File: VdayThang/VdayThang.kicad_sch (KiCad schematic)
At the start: 35 parts, among them SW1 SW_DIP_x01, U1 ATtiny85-20S

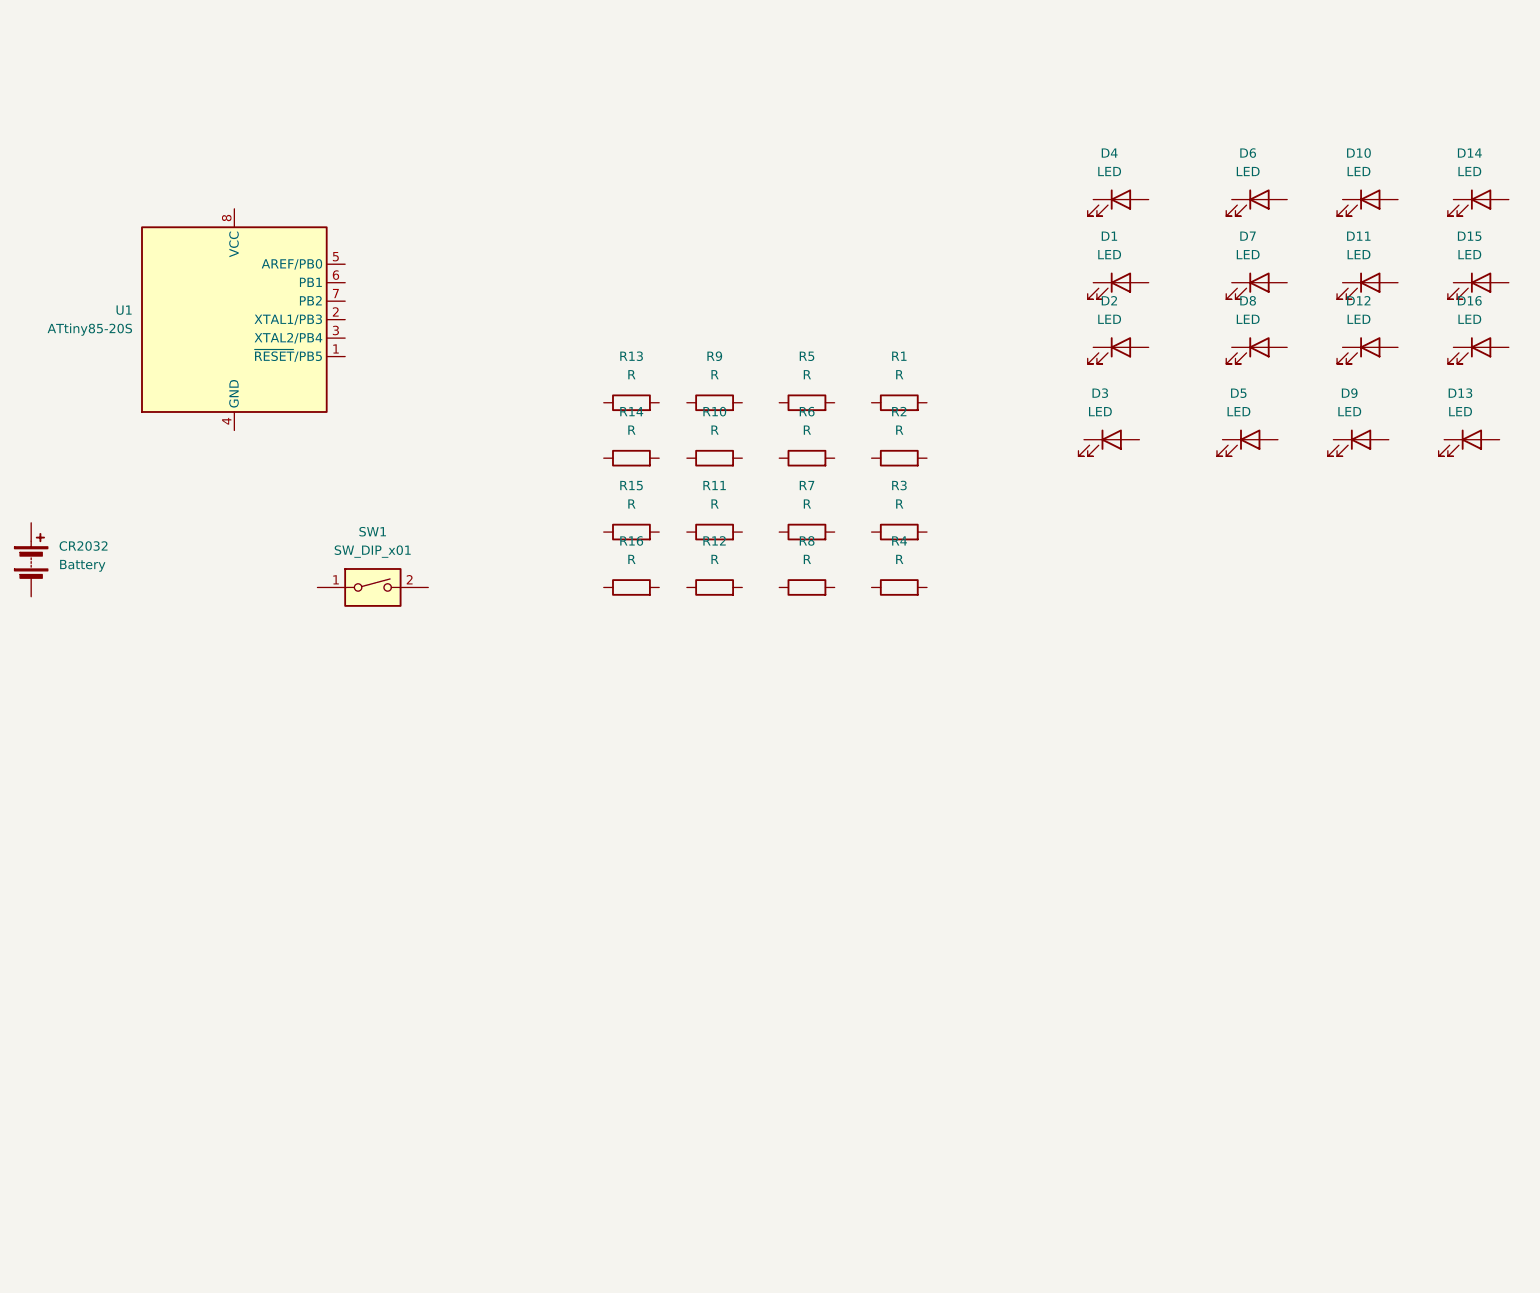
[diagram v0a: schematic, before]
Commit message: Schematic Mostly Done
Still need to assign footprints
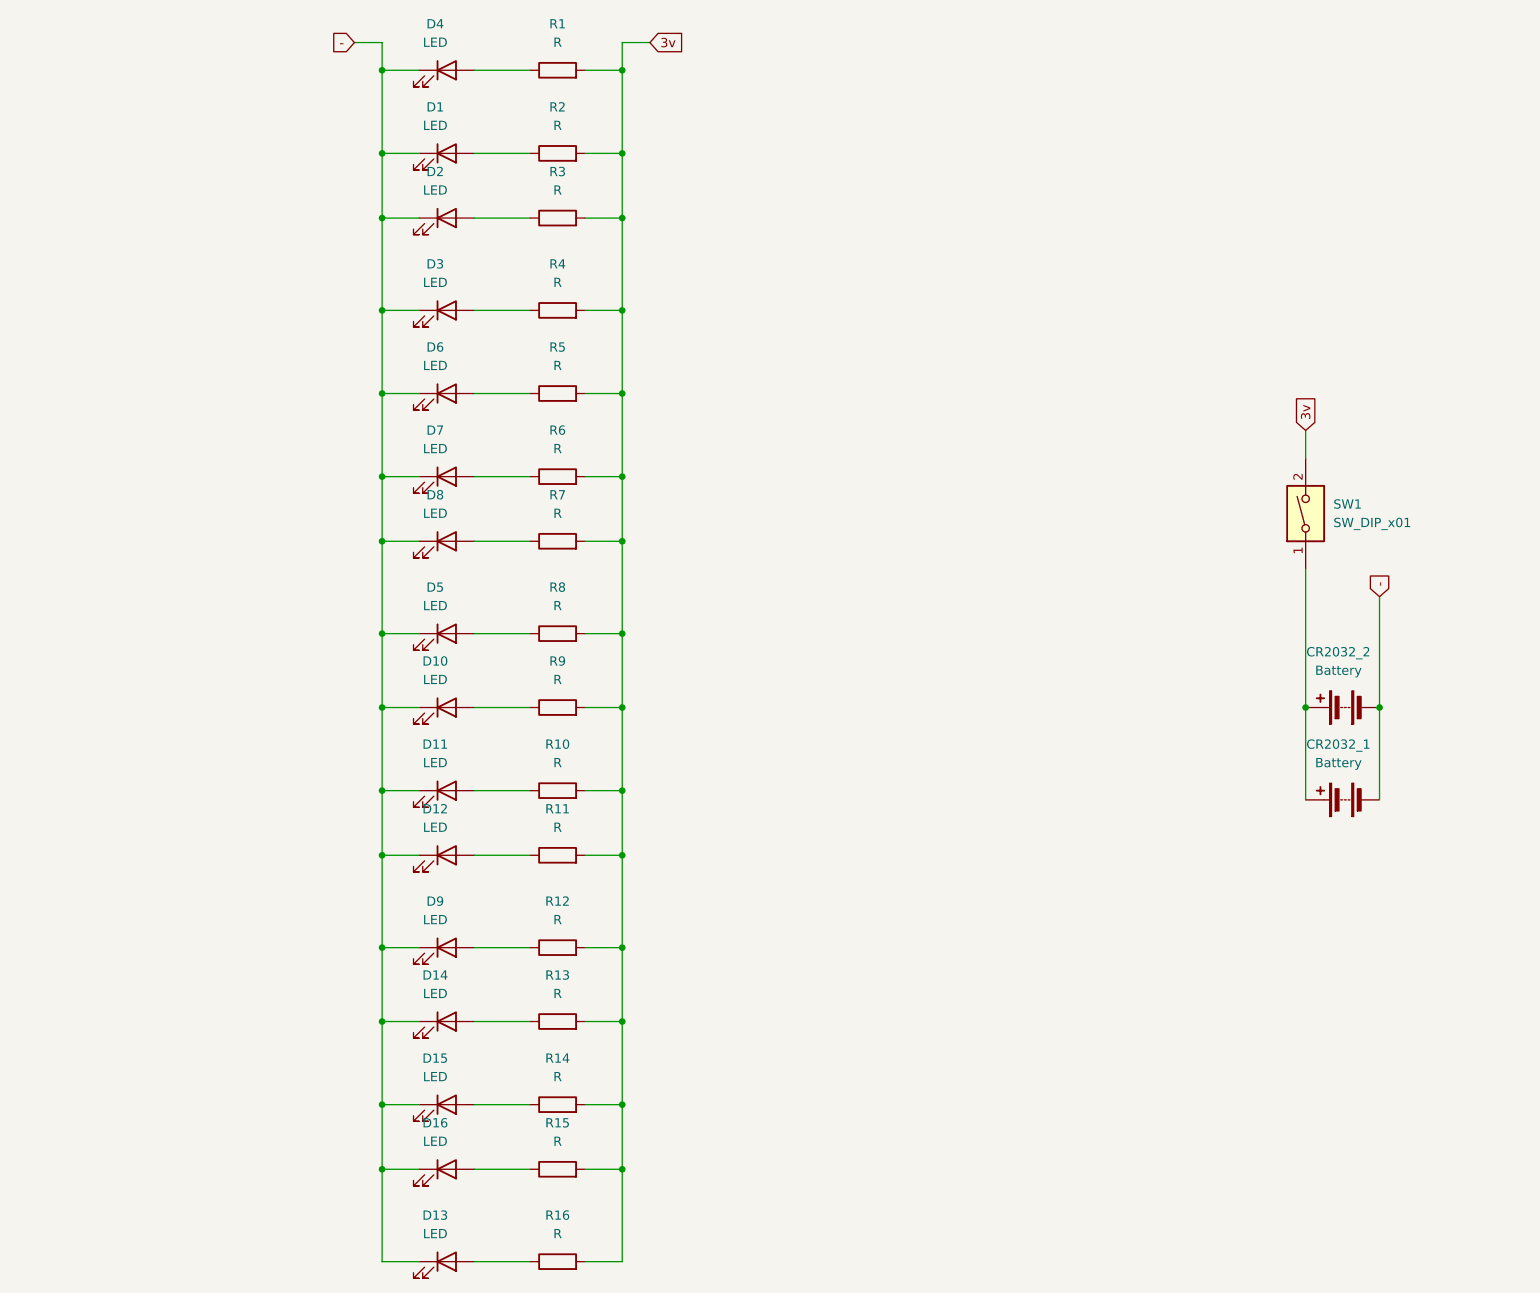
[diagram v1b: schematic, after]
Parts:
- removed U1: ATtiny85-20S, Package_SO:SOIC-8W_5.3x5.3mm_P1.27mm, symbol MCU_Microchip_ATtiny:ATtiny85-20S
- added CR2032_2: Battery, symbol Device:Battery
- renumbered CR2032 to CR2032_1
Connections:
- net -: now reaches D4.1 (K)
- net -: now also CR2032_1.2 (-), D1.1 (K), D10.1 (K), D11.1 (K), D12.1 (K), D13.1 (K), D14.1 (K), D15.1 (K), D16.1 (K), D2.1 (K), D3.1 (K), D5.1 (K), D6.1 (K), D7.1 (K), D8.1 (K), D9.1 (K), CR2032_2.2 (-)
- net at D4.2 (A): now also R1.1
- net at D1.2 (A): now also R2.1
- net at R12.1: now also D9.2 (A)
- net 3v: now reaches R12.2
- net 3v: now also R1.2, R10.2, R11.2, R13.2, R14.2, R15.2, R16.2, R2.2, R3.2, R4.2, R5.2, R6.2, R7.2, R8.2, R9.2, SW1.2
- net at D2.2 (A): now also R3.1
- net at CR2032_1.1 (+): now also SW1.1, CR2032_2.1 (+)
- net at R15.1: now also D16.2 (A)
- net at D7.2 (A): now also R6.1
- net at R5.1: now also D6.2 (A)
- net at D8.2 (A): now also R7.1
- net at D12.2 (A): now also R11.1
- net at R9.1: now also D10.2 (A)
- net at R13.1: now also D14.2 (A)
- net at R14.1: now also D15.2 (A)
- net at D11.2 (A): now also R10.1
- net at R8.1: now also D5.2 (A)
- net at R4.1: now also D3.2 (A)
- net at R16.1: now also D13.2 (A)
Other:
- title: (none) -> LED Heart
- moved on the sheet: CR2032_1, D1, D10, D11, D12, D13, D14, D15, D16, D2, D3, D4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

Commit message: assigned footprints
assigned footprints
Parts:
- removed SW1: SW_DIP_x01, symbol Switch:SW_DIP_x01
- added S1: SLW-66527511-SMT-TR, LogansCustom:SW_SLW-66527511-SMT-TR, symbol logancustom:SLW-66527511-SMT-TR
- CR2032_1, CR2032_2: footprint (none) -> LogansCustom:BAT_CR2032
- D1, D10, D11, D12, D13, D14, D15, D16, D2, D3, D4, D5, D6, D7, D8, D9: footprint (none) -> LED_SMD:LED_0805_2012Metric
- R1, R10, R11, R12, R13, R14, R15, R16, R2, R3, R4, R5, R6, R7, R8, R9: footprint (none) -> Resistor_SMD:R_0805_2012Metric
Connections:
- net 3v: now also S1.3
- net at CR2032_1.1 (+), CR2032_2.1 (+): now also S1.2

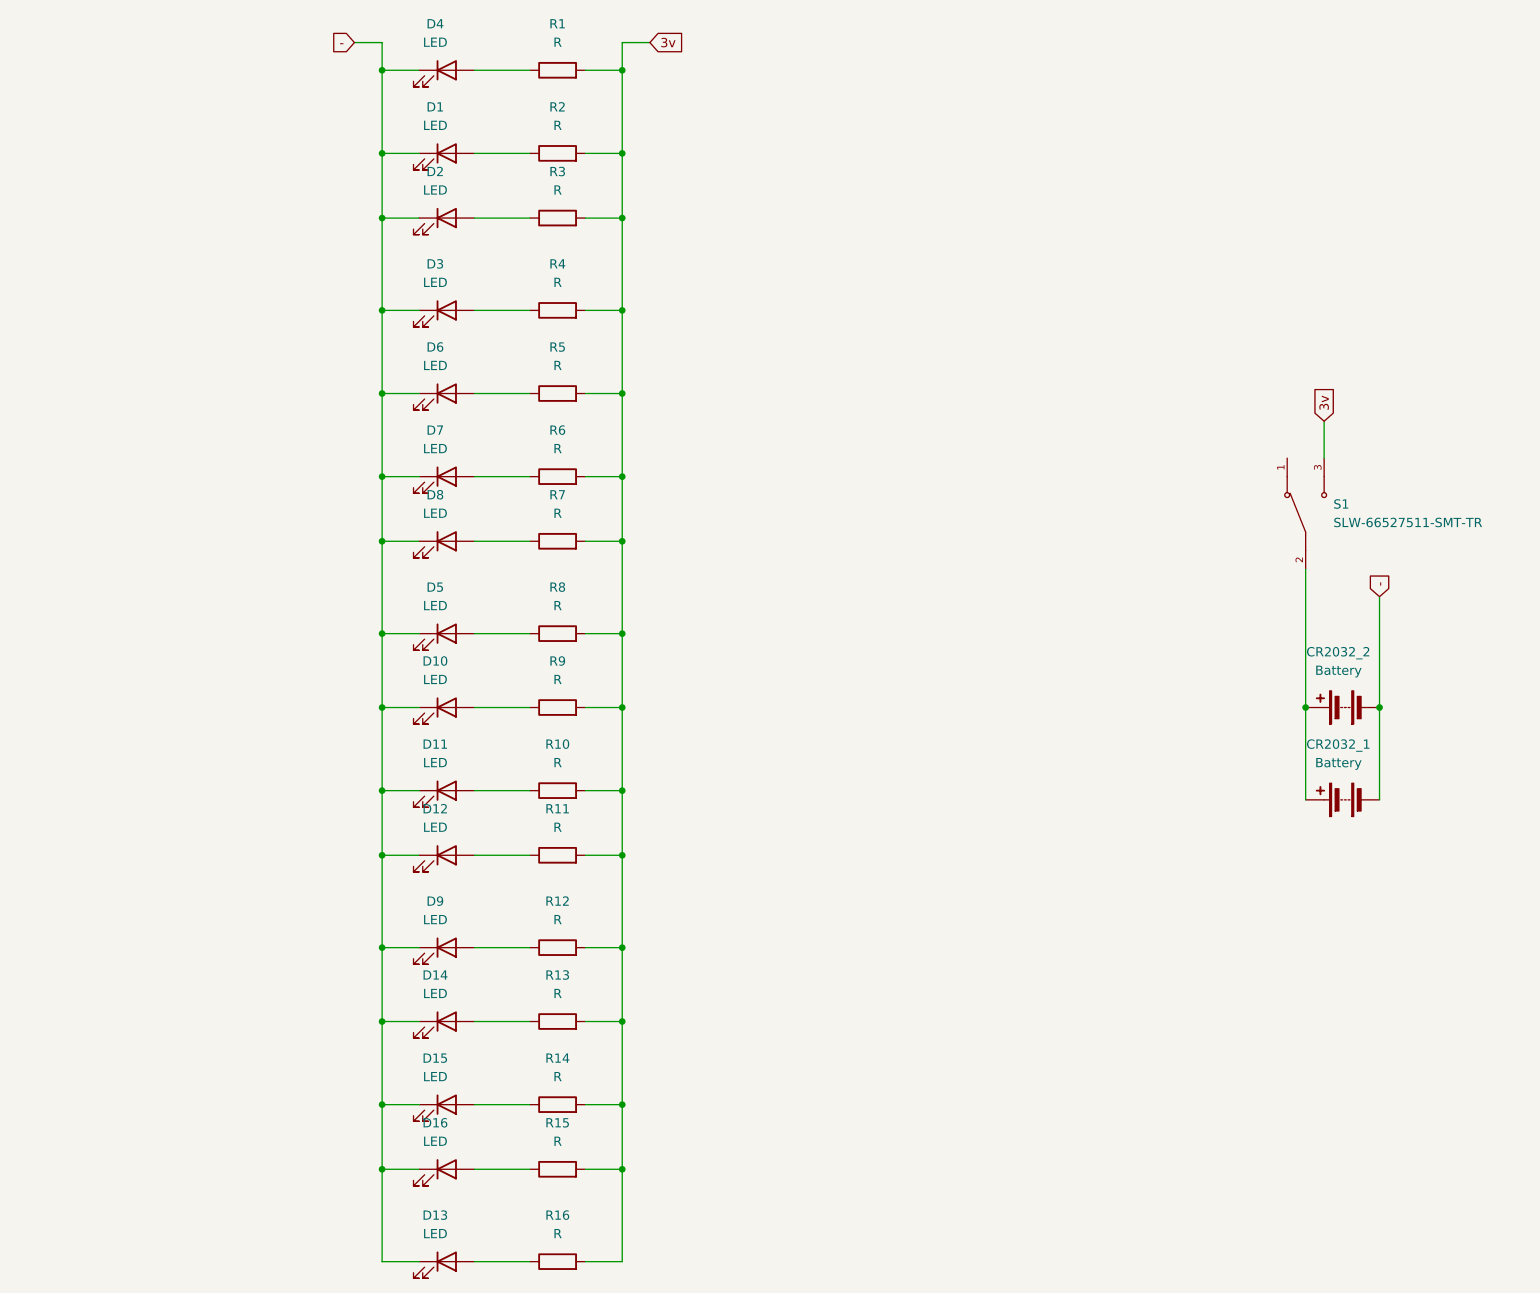
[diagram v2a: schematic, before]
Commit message: Routing and Footprints done
Finished routing board, made cr2032 holder footprint. Still need to add edge cuts.
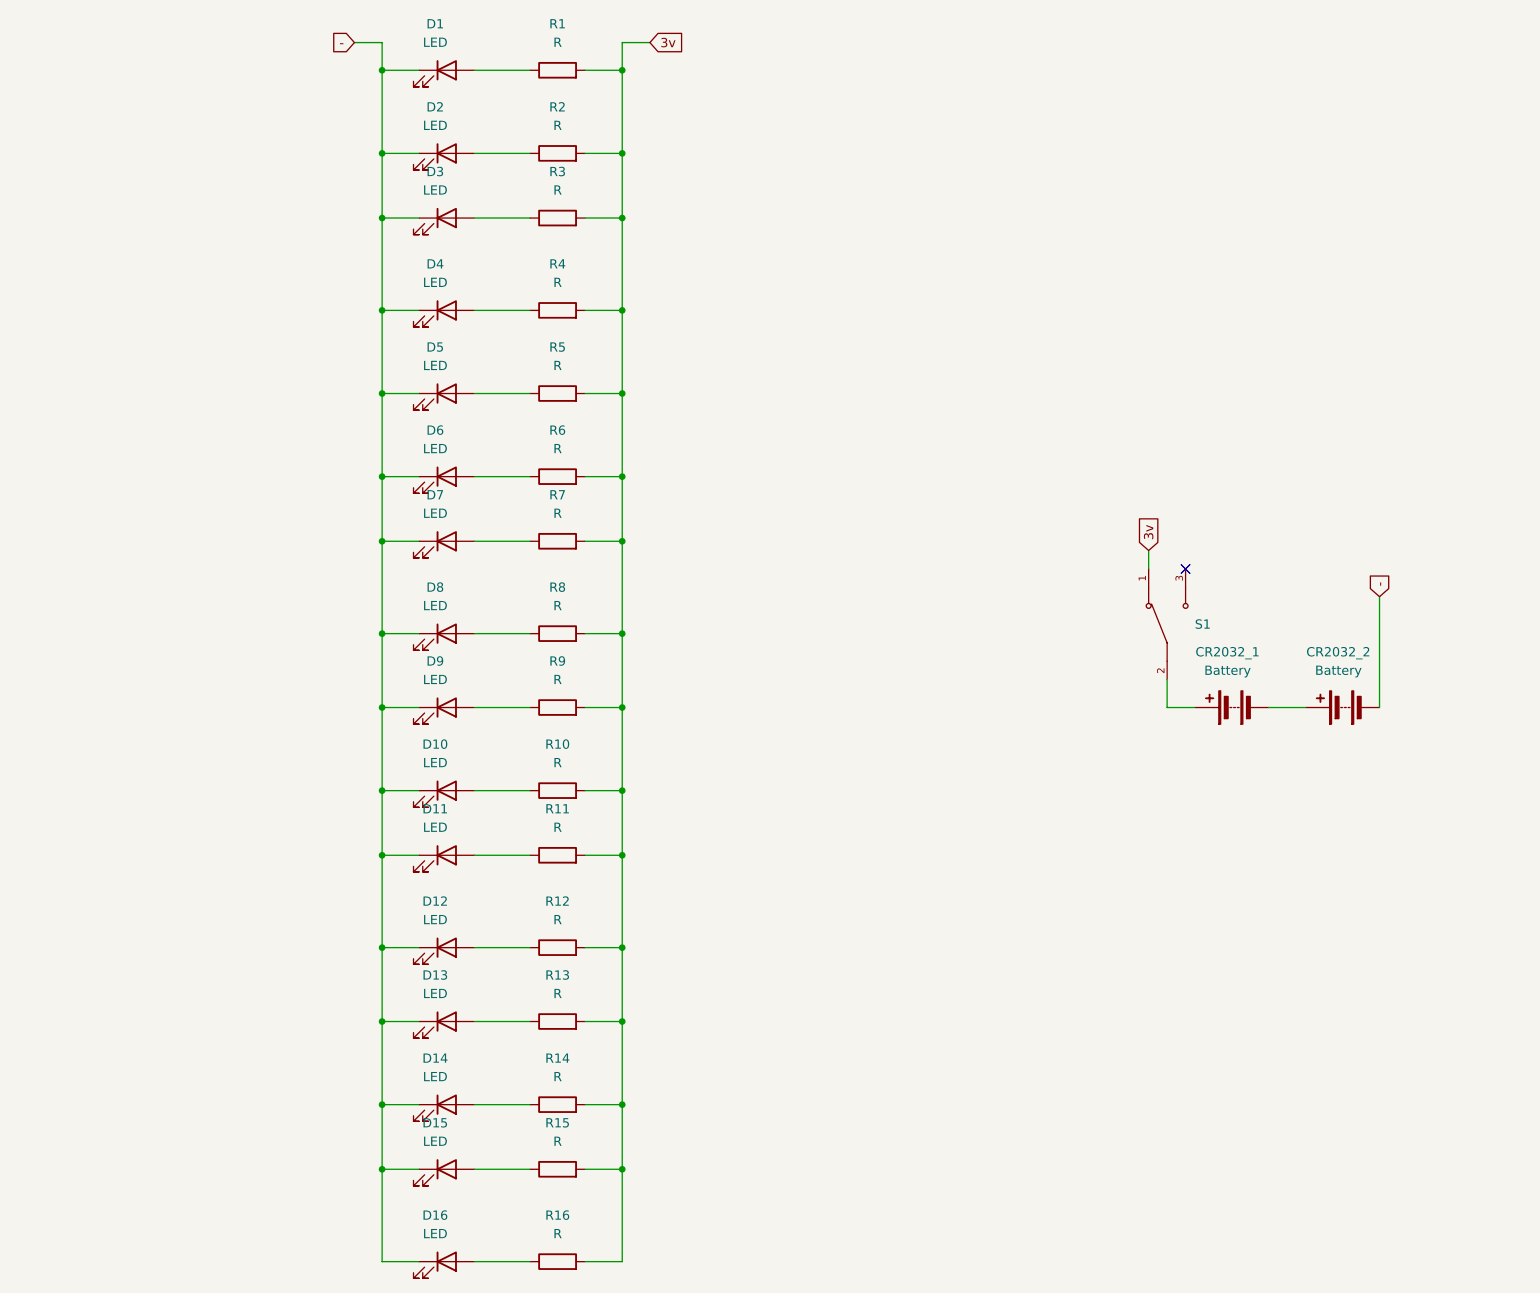
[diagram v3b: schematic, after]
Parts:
- S1: value SLW-66527511-SMT-TR -> ~
- renumbered D4 to D1, D11 to D10, D12 to D11, D9 to D12, D14 to D13, D15 to D14, D16 to D15, D13 to D16, D1 to D2, D2 to D3, D3 to D4, D6 to D5, D7 to D6, D8 to D7, D5 to D8, D10 to D9
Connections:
- net -: no longer CR2032_1.2 (-)
- net 3v: now also S1.1; no longer S1.3
- net at CR2032_1.1 (+), S1.2: no longer CR2032_2.1 (+)
- new net: CR2032_1.2 (-), CR2032_2.1 (+)
- no-connect marks 0 -> 1
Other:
- moved on the sheet: CR2032_1, S1
